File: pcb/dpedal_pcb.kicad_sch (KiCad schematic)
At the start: 7 parts, among them SW1 SW_Push, SW2 SW_Push, SW3 SW_Push, SW4 SW_Push, SW5 SW_Push, SW6 SW_Push

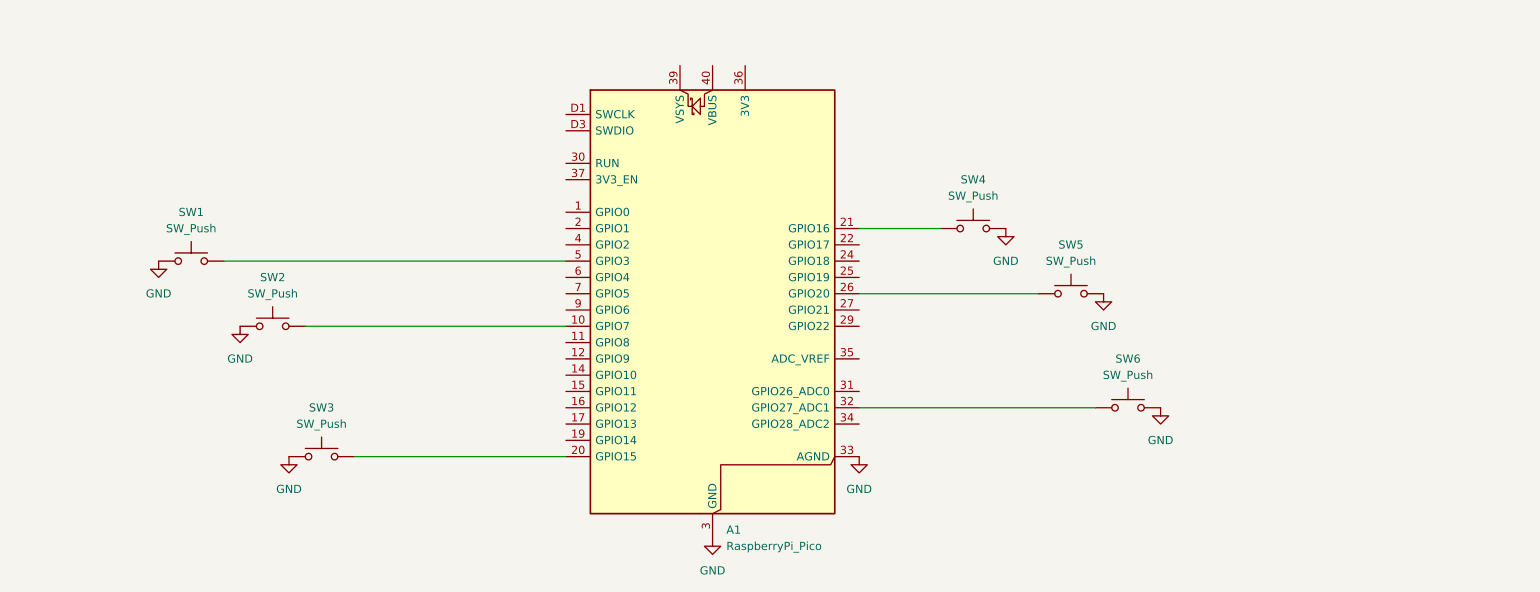
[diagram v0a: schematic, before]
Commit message: add step file to kicad export script
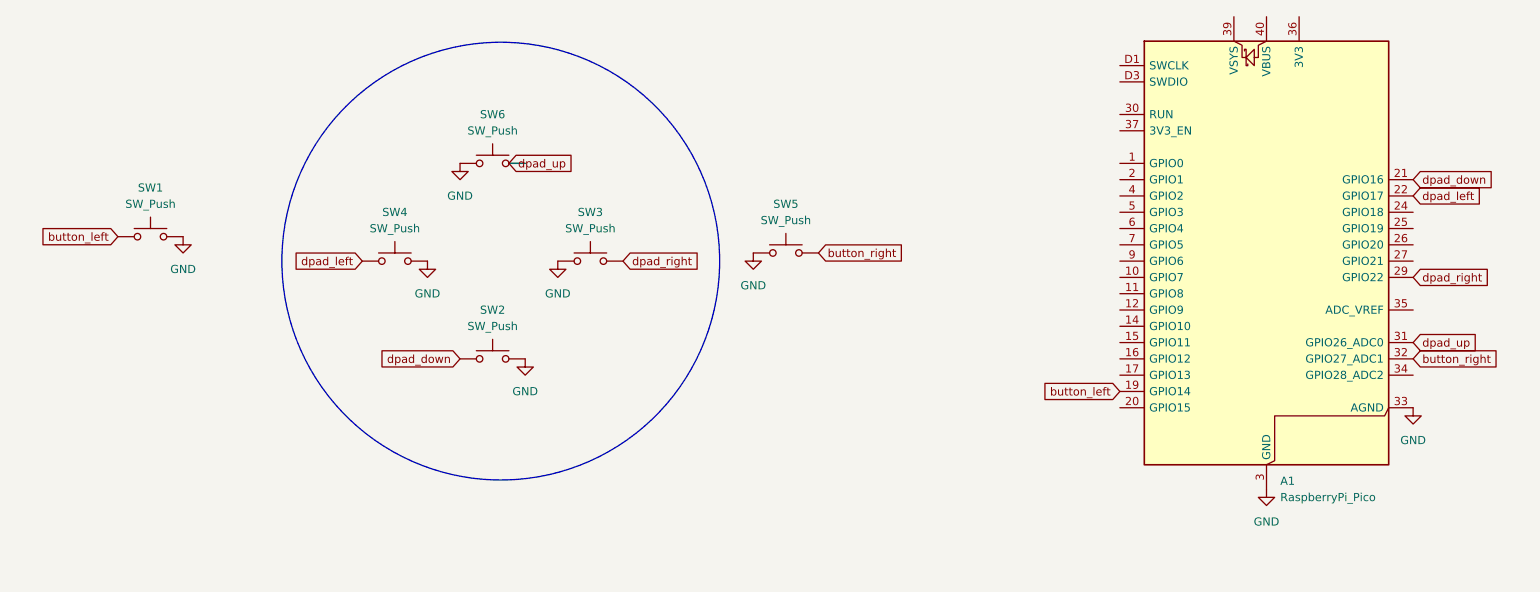
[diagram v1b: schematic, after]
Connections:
- net GND: now also SW1.2, SW2.2, SW5.1, SW6.1; no longer SW1.1, SW2.1, SW5.2, SW6.2
- net button_right: now reaches A1.32 (GPIO27_ADC1)
- net button_right: now also SW5.2; no longer SW6.1
- net at A1.20 (GPIO15): no longer SW3.2
- net at A1.10 (GPIO7): no longer SW2.2
- net at A1.26 (GPIO20): no longer SW5.1
- net at A1.5 (GPIO3): no longer SW1.2
- net button_left: now reaches A1.19 (GPIO14)
- net button_left: now also SW1.1
- net dpad_down: now reaches A1.21 (GPIO16)
- net dpad_down: now also SW2.1; no longer SW4.1
- net dpad_left: now reaches A1.22 (GPIO17)
- net dpad_left: now also SW4.1
- net dpad_right: now reaches A1.29 (GPIO22)
- net dpad_right: now also SW3.2
- net dpad_up: now reaches A1.31 (GPIO26_ADC0)
- net dpad_up: now also SW6.2
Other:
- moved on the sheet: A1, SW1, SW2, SW3, SW4, SW5, SW6

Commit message: fix erc/drc
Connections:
- no-connect marks 0 -> 28
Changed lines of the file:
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@@
+		)
+	)
+	(no_connect
+		(at 180.34 69.85)
+	)
+	(no_connect
+		(at 226.06 74.93)
+	)
+	(no_connect
+		(at 180.34 92.71)
+	)
+	(no_connect
+		(at 203.2 36.83)
+	)
+	(no_connect
+		(at 226.06 67.31)
+	)
+	(no_connect
+		(at 180.34 62.23)
+	)
+	(no_connect
+		(at 180.34 74.93)
+	)
+	(no_connect
+		(at 226.06 82.55)
+	)
+	(no_connect
+		(at 208.28 36.83)
+	)
+	(no_connect
+		(at 226.06 69.85)
+	)
+	(no_connect
+		(at 180.34 97.79)
+	)
+	(no_connect
+		(at 180.34 77.47)
+	)
+	(no_connect
+		(at 180.34 90.17)
+	)
+	(no_connect
+		(at 198.12 36.83)
+	)
+	(no_connect
+		(at 180.34 54.61)
+	)
+	(no_connect
+		(at 180.34 72.39)
+	)
+	(no_connect
+		(at 180.34 80.01)
+	)
+	(no_connect
+		(at 226.06 72.39)
+	)
+	(no_connect
+		(at 180.34 82.55)
+	)
+	(no_connect
+		(at 180.34 67.31)
+	)
+	(no_connect
+		(at 180.34 64.77)
+	)
+	(no_connect
+		(at 180.34 59.69)
+	)
+	(no_connect
+		(at 226.06 92.71)
+	)
+	(no_connect
+		(at 180.34 44.45)
+	)
+	(no_connect
+		(at 180.34 46.99)
+	)
+	(no_connect
+		(at 180.34 85.09)
+	)
+	(no_connect
+		(at 180.34 87.63)
+	)
+	(no_connect
+		(at 180.34 52.07)
+	)
+	(wire
+		(pts
+			(xy 203.2 116.84) (xy 203.2 110.49)
+		)
+		(stroke
+			(width 0)
+			(type default)
 		)
 	)
@@
 		(pts
 			(xy 85.09 59.69) (xy 87.63 59.69)
+		)
+		(stroke
+			(width 0)
+			(type default)
+		)
+	)
+	(wire
+		(pts
+			(xy 196.85 116.84) (xy 203.2 116.84)
 		)
 		(stroke
@@
 	(symbol
 		(lib_id "power:GND")
-		(at 203.2 110.49 0)
+		(at 196.85 116.84 0)
 		(unit 1)
 		(exclude_from_sim no)
@@
 		(dnp no)
 		(property "Reference" "#PWR03"
-			(at 203.2 116.84 0)
+			(at 196.85 123.19 0)
 			(effects
 				(font
@@
 		)
 		(property "Value" "GND"
-			(at 203.2 115.57 0)
+			(at 196.85 121.92 0)
 			(effects
 				(font
@@
 		)
 		(property "Footprint" ""
-			(at 203.2 110.49 0)
+			(at 196.85 116.84 0)
 			(effects
 				(font
@@
 		)
 		(property "Datasheet" ""
-			(at 203.2 110.49 0)
+			(at 196.85 116.84 0)
 			(effects
 				(font
@@
 		)
 		(property "Description" "Power symbol creates a global label with name \"GND\" , ground"
-			(at 203.2 110.49 0)
+			(at 196.85 116.84 0)
 			(effects
 				(font
@@
 		)
 		(pin "33"
+			(alternate "GND")
 		)
 		(pin "15"

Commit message: tweak pcb
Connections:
- net button_left: now also A1.17 (GPIO13); no longer A1.19 (GPIO14)
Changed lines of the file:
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@@
-	)
-	(no_connect
-		(at 180.34 92.71)
 	)
 	(no_connect
@@
 	(no_connect
 		(at 226.06 92.71)
+	)
+	(no_connect
+		(at 180.34 95.25)
 	)
 	(no_connect
@@
 	(global_label "button_left"
 		(shape input)
-		(at 180.34 95.25 180)
+		(at 180.34 92.71 180)
 		(fields_autoplaced yes)
 		(effects
@@
 		)
 		(property "Intersheetrefs" "${INTERSHEET_REFS}"
-			(at 167.1346 95.25 0)
-			(effects
-				(font
+			(at 167.1346 92.71 0)
+			(effects
+				(font

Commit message: silkscreen
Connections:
- net GND: now also SW4.1; no longer SW4.2
- net dpad_left: now also SW4.2; no longer SW4.1
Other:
- moved on the sheet: SW4
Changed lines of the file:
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@@
 	(global_label "dpad_left"
 		(shape input)
-		(at 62.23 74.93 180)
+		(at 64.77 76.2 0)
 		(fields_autoplaced yes)
 		(effects
@@
 				(size 1.27 1.27)
 			)
-			(justify right)
+			(justify left)
 		)
 		(property "Intersheetrefs" "${INTERSHEET_REFS}"
-			(at 50.476 74.93 0)
-			(effects
-				(font
-					(size 1.27 1.27)
-				)
-				(justify right)
+			(at 76.524 76.2 0)
+			(effects
+				(font
+					(size 1.27 1.27)
+				)
+				(justify left)
 				(hide yes)
 			)
@@
 	(symbol
 		(lib_id "power:GND")
-		(at 72.39 74.93 0)
+		(at 54.61 76.2 0)
 		(unit 1)
 		(exclude_from_sim no)
@@
 		(dnp no)
 		(property "Reference" "#PWR06"
-			(at 72.39 81.28 0)
+			(at 54.61 82.55 0)
 			(effects
 				(font
@@
 		)
 		(property "Value" "GND"
-			(at 72.39 80.01 0)
+			(at 54.61 81.28 0)
 			(effects
 				(font
@@
 		)
 		(property "Footprint" ""
-			(at 72.39 74.93 0)
+			(at 54.61 76.2 0)
 			(effects
 				(font
@@
 		)
 		(property "Datasheet" ""
-			(at 72.39 74.93 0)
+			(at 54.61 76.2 0)
 			(effects
 				(font
@@
 		)
 		(property "Description" "Power symbol creates a global label with name \"GND\" , ground"
-			(at 72.39 74.93 0)
+			(at 54.61 76.2 0)
 			(effects
 				(font
@@
 	(symbol
 		(lib_id "Switch:SW_Push")
-		(at 67.31 74.93 0)
+		(at 59.69 76.2 0)
 		(unit 1)
 		(exclude_from_sim no)
@@
 		(fields_autoplaced yes)
 		(property "Reference" "SW4"
-			(at 67.31 67.31 0)
+			(at 59.69 68.58 0)
 			(effects
 				(font
@@
 		)
 		(property "Value" "SW_Push"
-			(at 67.31 69.85 0)
+			(at 59.69 71.12 0)
 			(effects
 				(font
@@
 		)
 		(property "Footprint" "PCM_Switch_Keyboard_Hotswap_Kailh:SW_Hotswap_Kailh_Choc_V1"
-			(at 67.31 69.85 0)
+			(at 59.69 71.12 0)
 			(effects
 				(font
@@
 		)
 		(property "Datasheet" "~"
-			(at 67.31 69.85 0)
+			(at 59.69 71.12 0)
 			(effects
 				(font
@@
 		)
 		(property "Description" "Push button switch, generic, two pins"
-			(at 67.31 74.93 0)
-			(effects
-				(font
+			(at 59.69 76.2 0)
+			(effects
+				(font
